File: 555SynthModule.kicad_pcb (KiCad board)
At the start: 2 copper layers, 64.8 x 34.3 mm, 32 parts, among them J1 Conn_01x09_Male, Q1 2N3904, Q2 2N3904, Q3 2N3904, Q4 2N3904, Q5 2N3904, U1 NE555P, U2 LM741

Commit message: Labeled module header pins
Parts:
- moved C7 1.91 mm to (156.8, 83.8)
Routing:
- net +15V: track 6.78 -> 0.00 mm
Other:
- board text added: "+15V"
- board text added: "-15V"
- board text added: "EN"
- board text added: "GND"
- board text added: "OUT"
- board text added: "RA0"
- board text added: "RA1"
- board text added: "RA2"
- board text added: "RA3"

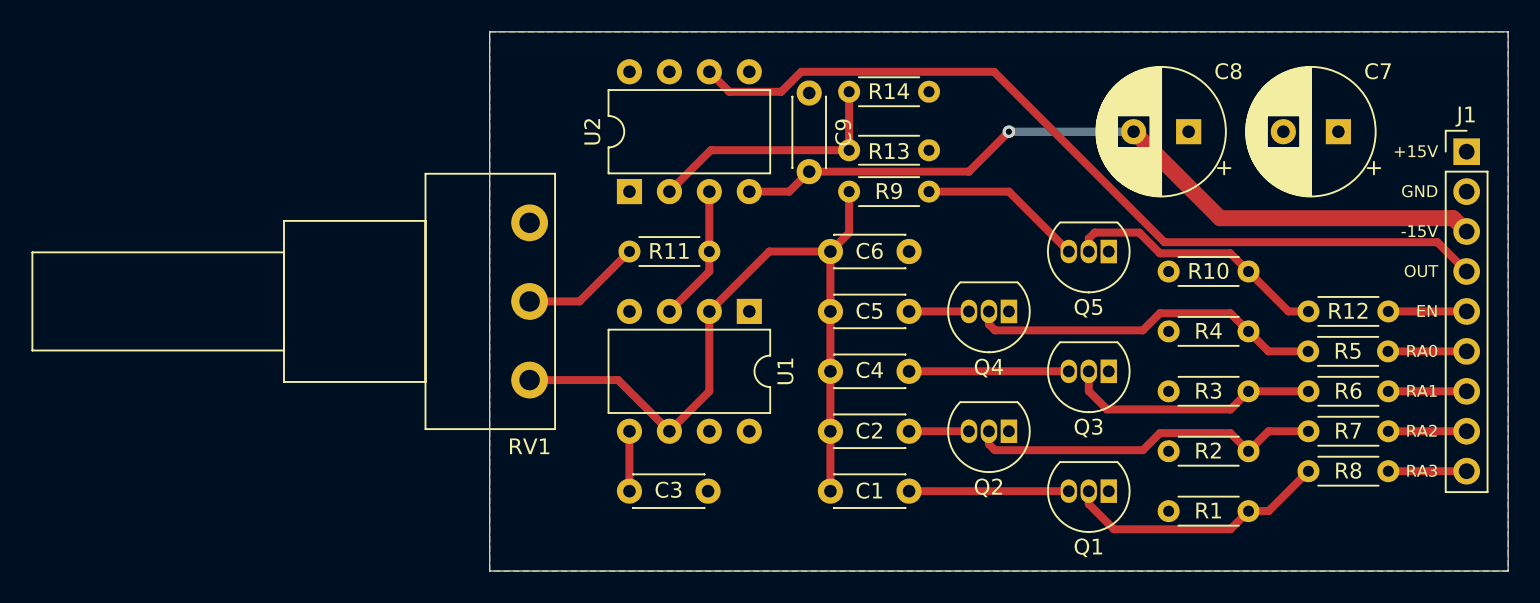
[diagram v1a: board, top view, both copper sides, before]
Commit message: Added teardrops
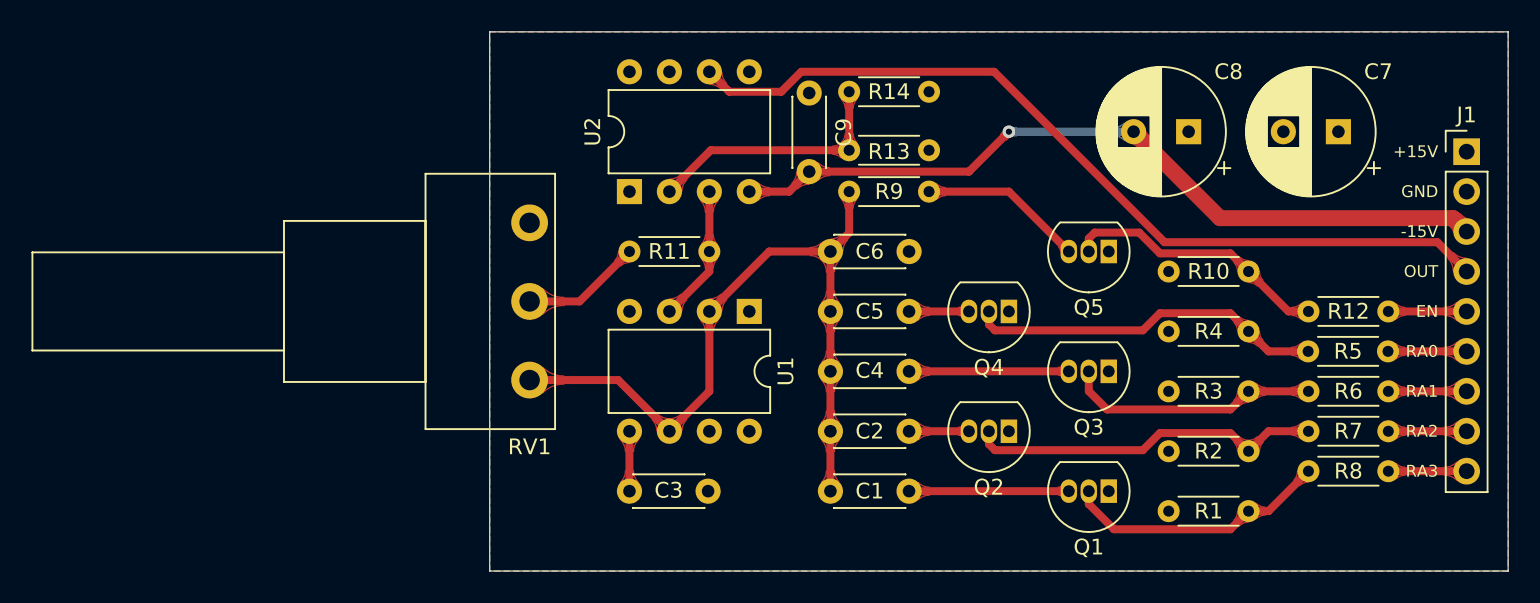
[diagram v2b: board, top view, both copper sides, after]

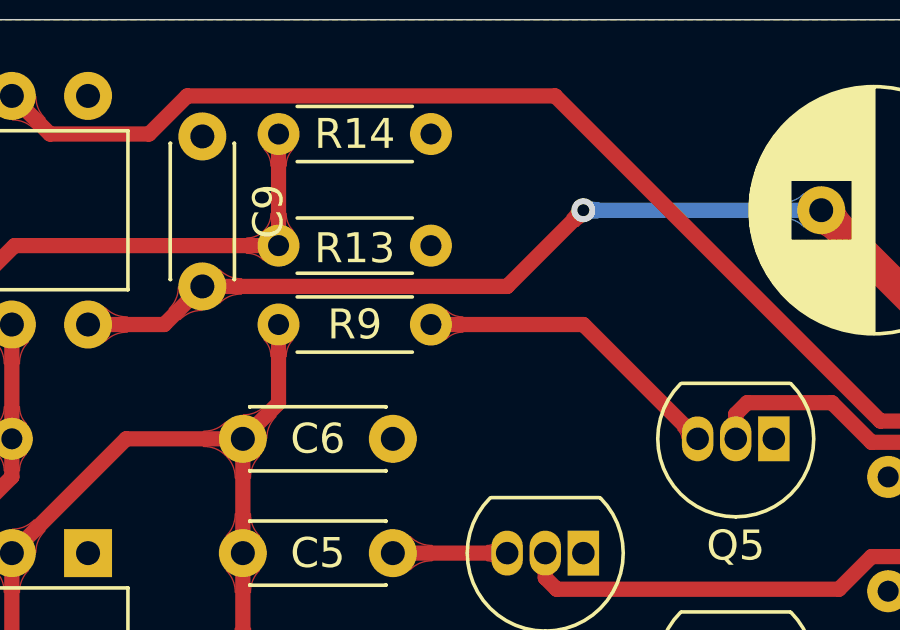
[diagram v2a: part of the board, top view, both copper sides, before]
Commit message: Added Gerber files, fixed unconnected trace
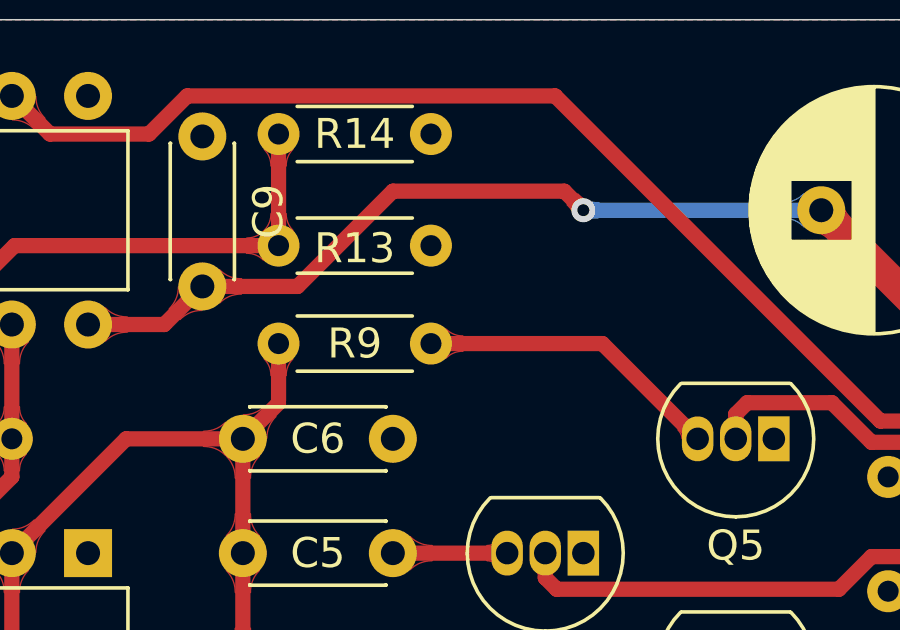
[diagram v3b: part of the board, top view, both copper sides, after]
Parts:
- moved R9 0.64 mm to (125.7, 88.3)
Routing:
- net Net-(C1-Pad1): track 47.8 -> 47.1 mm
- net -15V: track 49.8 -> 50.4 mm
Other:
- rule pad_to_mask_clearance: 0.05 -> 0.0508
- rule trace_min: 0.2 -> 0.16
- rule via_min_size: 0.4 -> 0.6

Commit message: Updated gerbers, minor changes
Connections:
- net /ENABLE renamed /DISABLE
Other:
- board text added: "555 Oscillator - Ray Clemens 2020"
- board text added: "DE"
- board text removed: "EN"
